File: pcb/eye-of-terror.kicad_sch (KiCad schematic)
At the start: 226 parts, among them J1 Conn_01x02_Socket, J2 G-Switch GT-USB-7055E, J3 Conn_01x04, J4 Conn_01x04, J5 Conn_01x03, J6 Conn_01x02_Socket, J7 Conn_01x02_Socket, J8 Conn_01x03, Q1 IPT020N10N3, Q10 ALS-PT19-315C/L177/TR8, Q11 ALS-PT19-315C/L177/TR8, Q12 ALS-PT19-315C/L177/TR8, Q13 ALS-PT19-315C/L177/TR8, Q14 ALS-PT19-315C/L177/TR8, Q15 ALS-PT19-315C/L177/TR8, Q16 ALS-PT19-315C/L177/TR8, Q2 IPT020N10N3, Q3 IPT020N10N3, Q4 IPT020N10N3, Q5 IPT020N10N3, Q6 IPT020N10N3, Q7 ALS-PT19-315C/L177/TR8, Q8 ALS-PT19-315C/L177/TR8, Q9 ALS-PT19-315C/L177/TR8, SW1 SW_Push, SW2 SW_Push, U1 RP2350B, U2 TD1660, U3 AP63205WU-7, U4 LSM6DS3, U5 W25Q32JVSS, U7 DRV8353HRTAR, Y1 ABM8-272-T3

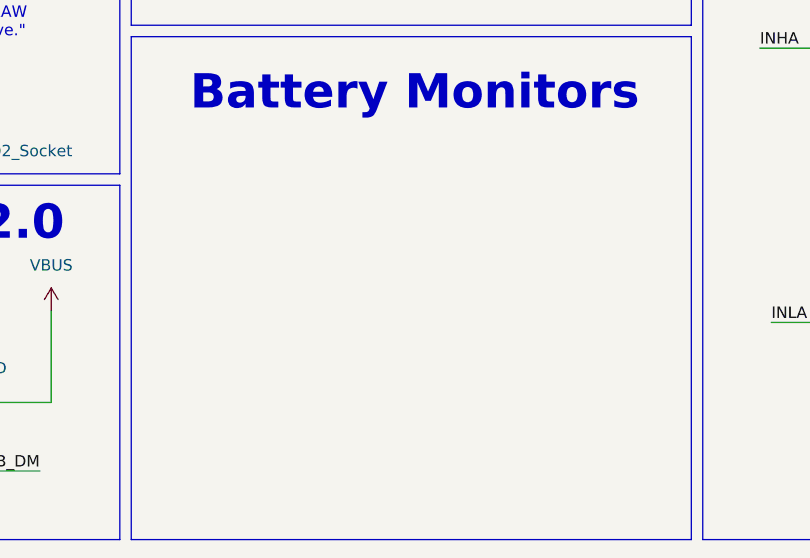
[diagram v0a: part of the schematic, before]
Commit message: added voltage dividers for battery measurement back because I think for now it's still the simplest option
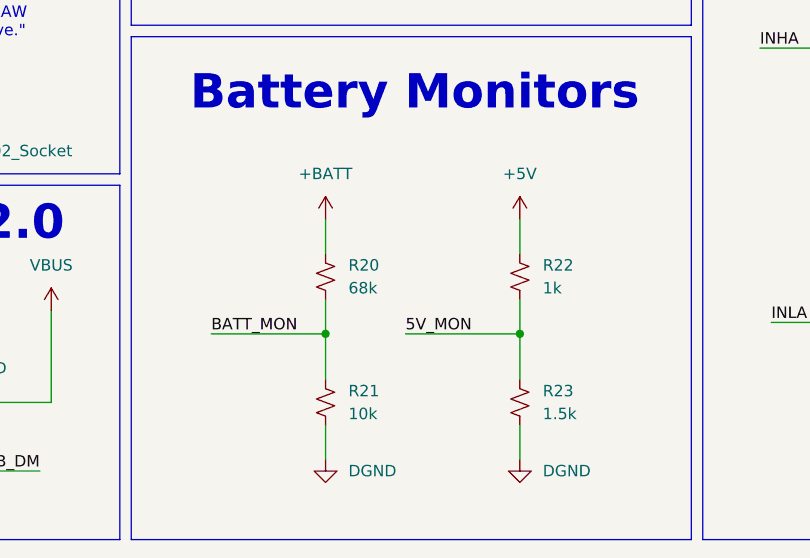
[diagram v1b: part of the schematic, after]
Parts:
- added R20: 68k, Resistor_SMD:R_0603_1608Metric, symbol Device:R_Small_US
- added R21: 10k, Resistor_SMD:R_0402_1005Metric, symbol Device:R_Small_US
- added R22: 1k, Resistor_SMD:R_0402_1005Metric, symbol Device:R_Small_US
- added R23: 1.5k, Resistor_SMD:R_1210_3225Metric, symbol Device:R_Small_US
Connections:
- net +5V: now also R22.1
- net +BATT: now also R20.1
- net 5V_MON: now also R22.2, R23.1
- net BATT_MON: now also R20.2, R21.1
- net DGND: now also R21.2, R23.2

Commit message: BOM fully updated, added diodes
* added another Schottky diode for USB backfeed from 5V line
* added ESD protection to USB data lines
* for some reason, LCSC numbers disappeared (i forgot if they were ever
  there), so LCSC numbers added
* BOM in schematic matches BOM in Notion
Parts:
- added D9: SS36, Diode_SMD:D_SMB, symbol Diode:SS36
- added JP17: SolderJumper_2_Bridged, Jumper:SolderJumper-2_P1.3mm_Bridged_RoundedPad1.0x1.5mm, symbol Jumper:SolderJumper_2_Bridged
- added TP10: TestPoint, symbol Connector:TestPoint
- added U8: ESD122DMXR, ESD122DMXR:IC_ESD122DMXR, symbol ESD122:ESD122DMXR
- C1, C39: LCSC Number (none) -> C72487
- C10, C11, C14, C15, C17, C21, C22, C23, C24, C25, C26, C27, C28, C29: LCSC Number (none) -> C60474
- C12, C13: LCSC Number (none) -> C86285
- C16, C18, C19, C20, C8: LCSC Number (none) -> C23733
- C2, C30, C36, C37, C38, C9: LCSC Number (none) -> C14663
- C3, C4, C7: LCSC Number (none) -> C86295
- C31, C33, C34, C35: LCSC Number (none) -> C15849
- C32: LCSC Number (none) -> C368599
- C5: LCSC Number (none) -> C307451
- C6: LCSC Number (none) -> C62782
- D1: LCSC Number (none) -> C110904
- D13, D3, D5, D7: LCSC Number (none) -> C965825
- D16, D4, D6, D8: LCSC Number (none) -> C965827
- D18, D19, D20, D21, D22, D23, D24, D25, D26, D27, D28: LCSC Number (none) -> C2984265
- D2: LCSC Number (none) -> C35490
- J2: LCSC Number (none) -> C7450622
- L1: LCSC Number (none) -> C703747
- L2: LCSC Number (none) -> C2921170
- L3: LCSC Number (none) -> C42411119
- Q1, Q2, Q3, Q4, Q5, Q6: LCSC Number (none) -> C537070
- Q10, Q11, Q12, Q13, Q14, Q15, Q16, Q7, Q8, Q9: LCSC Number (none) -> C146233
- R1, R2: LCSC Number (none) -> C114759
- R10, R11, R15, R22, R8: LCSC Number (none) -> C106235
- R12: LCSC Number (none) -> C138002
- R13, R14: LCSC Number (none) -> C25100
- R16, R21, R43, R46, R48, R50, R55, R56, R57, R58, R63, R64, R9: LCSC Number (none) -> C60490
- R17, R18, R19: LCSC Number (none) -> C7467246
- R20: LCSC Number (none) -> C23231
- R23: LCSC Number (none) -> C3000602
- R25, R26, R27, R28, R29, R30, R35, R38: LCSC Number (none) -> C105588
- R3: LCSC Number (none) -> C105578
- R4: LCSC Number (none) -> C93947
- R40: LCSC Number (none) -> C22548
- R44, R45, R47, R49, R51, R52, R53, R54, R59, R60: LCSC Number (none) -> C163455
- R5: LCSC Number (none) -> C2907038
- R6: LCSC Number (none) -> C114065
- R7: LCSC Number (none) -> C114607
- SW1, SW2: LCSC Number (none) -> C720477
- TP1, TP2, TP3, TP4, TP5, TP6, TP7, TP8, TP9: now left out of the parts list
- U1: LCSC Number (none) -> C39843328
- U2: LCSC Number (none) -> C2832211
- U3: LCSC Number (none) -> C780769
- U4: LCSC Number (none) -> C95230
- U5: LCSC Number (none) -> C97521
- U7: LCSC Number (none) -> C1518717
- Y1: LCSC Number (none) -> C20625731
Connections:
- net +5V: now also JP17.2 (B)
- net DGND: now also TP10.1, U8.1 (GND)
- net USB_DM: now also U8.2 (IO1)
- net USB_DP: now also U8.3 (IO2)
- net VBUS: now also D9.1 (K), JP17.1 (A); no longer J2.A4/B9 (VBUS), J2.B4/A9 (VBUS)
- new net: D9.2 (A), J2.A4/B9 (VBUS), J2.B4/A9 (VBUS)
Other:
- note added: "Battery Monitor Voltage Dividers"
- note added: "EMI Shield"
- note added: "Power Config Jumpers"
- note added: "Short this jumper to power the board off of the 5V coming from the USB port. Do NOT plug in and use a battery while this jumper is shorted."
- note added: "USB ESD"
- note removed: "Battery Monitors"
- moved on the sheet: D3, D4, D5, D6, D7, D8, J1, J7, R20, R21, R22, R23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

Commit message: added footprints for motor winding connections
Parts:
- TP4, TP5, TP6, TP7, TP8, TP9: footprint (none) -> motor-phase-connection:THTPad_D5.0mm_Drill2.5mm
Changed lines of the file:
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@@
 			)
 		)
-		(property "Footprint" ""
+		(property "Footprint" "motor-phase-connection:THTPad_D5.0mm_Drill2.5mm"
 			(at 433.07 261.62 0)
 			(hide yes)
@@
 			)
 		)
-		(property "Footprint" ""
+		(property "Footprint" "motor-phase-connection:THTPad_D5.0mm_Drill2.5mm"
 			(at 416.56 261.62 0)
 			(hide yes)
@@
 			)
 		)
-		(property "Footprint" ""
+		(property "Footprint" "motor-phase-connection:THTPad_D5.0mm_Drill2.5mm"
 			(at 469.9 261.62 0)
 			(hide yes)
@@
 			)
 		)
-		(property "Footprint" ""
+		(property "Footprint" "motor-phase-connection:THTPad_D5.0mm_Drill2.5mm"
 			(at 461.01 276.86 0)
 			(hide yes)
@@
 			)
 		)
-		(property "Footprint" ""
+		(property "Footprint" "motor-phase-connection:THTPad_D5.0mm_Drill2.5mm"
 			(at 444.5 276.86 0)
 			(hide yes)
@@
 			)
 		)
-		(property "Footprint" ""
+		(property "Footprint" "motor-phase-connection:THTPad_D5.0mm_Drill2.5mm"
 			(at 486.41 261.62 0)
 			(hide yes)

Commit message: added nmos driver for encoder LEDs
and also backup solder jumper in case that doesn't work.
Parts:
- added JP18: SolderJumper_2_Bridged, Jumper:SolderJumper-2_P1.3mm_Bridged_RoundedPad1.0x1.5mm, symbol Jumper:SolderJumper_2_Open
- added Q17: NMOS, Package_TO_SOT_SMD:TSOT-23, symbol Transistor_FET_Other:Q_NMOS_Depletion_GSD
- added R24: 10k, Resistor_SMD:R_0402_1005Metric, symbol Device:R_Small_US
- JP17: symbol Jumper:SolderJumper_2_Bridged -> Jumper:SolderJumper_2_Open
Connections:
- net DGND: now also JP18.2 (B), Q17.2 (S); no longer R44.2, R45.2, R47.2, R49.2, R51.2, R52.2, R53.2, R54.2, R59.2, R60.2
- net ENC_LED_DRV: now reaches U1.47 (GPIO38)
- net ENC_LED_DRV: now also R24.1
- new net: Q17.1 (G), R24.2
- new net ENC_LED_OUT: JP18.1 (A), Q17.3 (D), R44.2, R45.2, R47.2, R49.2, R51.2, R52.2, R53.2, R54.2, R59.2, R60.2
- no-connect marks 10 -> 9
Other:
- note added: "Encoder LED Driver"
- note added: "If this NMOS driver doesn't work, or the V_SD is too high and the LEDs are too dim, short all the LEDs to ground with this jumper."
- moved on the sheet: TP4, TP5, TP6, TP7, TP8, TP9

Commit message: WIP time to do layout again
* moved some more stuff to the back of the board
* need to move more stuff
* deleted all traces and vias
* changed standard SMD footprints to hand-solder version
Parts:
- C10, C11, C12, C13, C14, C15, C16, C17, C18, C19, C20, C21, C22, C23, C24, C25, C26, C27, C28, C29, C32, C5, C8: footprint Capacitor_SMD:C_0402_1005Metric -> Capacitor_SMD:C_0402_1005Metric_Pad0.74x0.62mm_HandSolder
- C2, C3, C30, C31, C33, C34, C35, C36, C37, C38, C4, C6, C7, C9: footprint Capacitor_SMD:C_0603_1608Metric -> Capacitor_SMD:C_0603_1608Metric_Pad1.08x0.95mm_HandSolder
- D13, D16, D18, D19, D20, D21, D22, D23, D24, D25, D26, D27, D28, D3, D4, D5, D6, D7, D8: footprint Diode_SMD:D_1206_3216Metric -> Diode_SMD:D_1206_3216Metric_Pad1.42x1.75mm_HandSolder
- Q10, Q11, Q12, Q13, Q14, Q15, Q16, Q7, Q8, Q9: footprint LED_SMD:LED_0603_1608Metric -> LED_SMD:LED_0603_1608Metric_Pad1.05x0.95mm_HandSolder
- Q17: footprint Package_TO_SOT_SMD:TSOT-23 -> Package_TO_SOT_SMD:TSOT-23_HandSoldering
- R1, R10, R11, R12, R13, R14, R15, R16, R2, R21, R22, R24, R4, R43, R44, R45, R46, R47, R48, R49, R50, R51, R52, R53, R54, R55, R56, R57, R58, R59, R60, R63, R64, R8, R9: footprint Resistor_SMD:R_0402_1005Metric -> Resistor_SMD:R_0402_1005Metric_Pad0.72x0.64mm_HandSolder
- R17, R18, R19: footprint Resistor_SMD:R_1206_3216Metric -> Resistor_SMD:R_1206_3216Metric_Pad1.30x1.75mm_HandSolder
- R20, R25, R26, R27, R28, R29, R3, R30, R35, R38, R5, R6, R7: footprint Resistor_SMD:R_0603_1608Metric -> Resistor_SMD:R_0603_1608Metric_Pad0.98x0.95mm_HandSolder
- R23: footprint Resistor_SMD:R_1210_3225Metric -> Resistor_SMD:R_1210_3225Metric_Pad1.30x2.65mm_HandSolder
- R40: footprint Resistor_SMD:R_1210_3225Metric -> Resistor_SMD:R_0603_1608Metric_Pad0.98x0.95mm_HandSolder

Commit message: WIP layout
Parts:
- added JP19, JP20, JP21, JP22, JP23, JP24: SolderJumper_2_Bridged, Jumper:SolderJumper-2_P1.3mm_Bridged_RoundedPad1.0x1.5mm, symbol Jumper:SolderJumper_2_Bridged
- JP17: footprint Jumper:SolderJumper-2_P1.3mm_Bridged_RoundedPad1.0x1.5mm -> Jumper:SolderJumper-2_P1.3mm_Open_RoundedPad1.0x1.5mm
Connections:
- net GPIO0: now also JP19.1 (A); no longer R9.2, U5.1 (~{CS})
- net QSPI_SCLK: now also JP20.1 (A); no longer U5.6 (CLK)
- net QSPI_SD0: now also JP21.1 (A); no longer U5.5 (DI/IO_{0})
- net QSPI_SD1: now also JP22.1 (A); no longer U5.2 (DO/IO_{1})
- net QSPI_SD2: now also JP23.1 (A); no longer U5.3 (~{WP}/IO_{2})
- net QSPI_SD3: now also JP24.1 (A); no longer U5.7 (~{HOLD}/~{RESET}/IO_{3})
- new net: JP23.2 (B), U5.3 (~{WP}/IO_{2})
- new net: JP19.2 (B), R9.2, U5.1 (~{CS})
- new net: JP22.2 (B), U5.2 (DO/IO_{1})
- new net: JP20.2 (B), U5.6 (CLK)
- new net: JP21.2 (B), U5.5 (DI/IO_{0})
- new net: JP24.2 (B), U5.7 (~{HOLD}/~{RESET}/IO_{3})

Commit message: WIP layout almost done
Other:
- moved on the sheet: D3, D4, D5, D6, D7, D8, R25, R26, R27, R28, R29, R30

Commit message: WIP layout
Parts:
- added NT3: NetTie_2, NetTie:NetTie-2_SMD_Pad2.0mm, symbol Device:NetTie_2
- added TP11, TP12: TestPoint, TestPoint:TestPoint_Pad_D1.0mm, symbol Connector:TestPoint
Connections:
- net +3V3: now also TP11.1
- net +5V: now also TP12.1
- net DGND: now also NT3.2
- net PGND: now also NT3.1
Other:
- moved on the sheet: NT1, NT2
